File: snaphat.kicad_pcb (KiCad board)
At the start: 2 copper layers, 100 x 99.4 mm, 115 parts, among them J1 Conn_01x08_S8B-PH-K-S(LF)(SN), J10 P70-6000045R, J11 P70-6000045R, J12 P70-6000045R, J2 Conn_02x20_2214SM-40G-75-PCR, J3 Conn_01x02_B2B-PH-K-S(LF)(SN), J4 USB_C_USB4930-00-A, J5 Conn_01x03_MC34747, J6 Conn_01x04_SFV4R-3STBE1HLF/C, J7 Conn_01x04_SFV4R-3STBE1HLF/C, J8 P70-6000045R, J9 P70-6000045R, Q1 Q_BC817-25, Q2 Q_FDC6561AN, SW1 SW_B3FS-1050, SW2 SW_B3FS-1050, SW3 SW_B3FS-1050, SW4 SW_B3FS-1050, SW5 SW_B3FS-1050, SW6 SW_B3FS-1050, SW7 SW_B3FS-1050, SW8 SW_B3F-3150, SW9 1825232-1, U1 INA219BIDR, U2 MIC2250-1YD5-TR, U3 MCP73871T-2CCI/ML, U5 AP9101CAK6-ABTRG1, U6 LIS2DW12TR

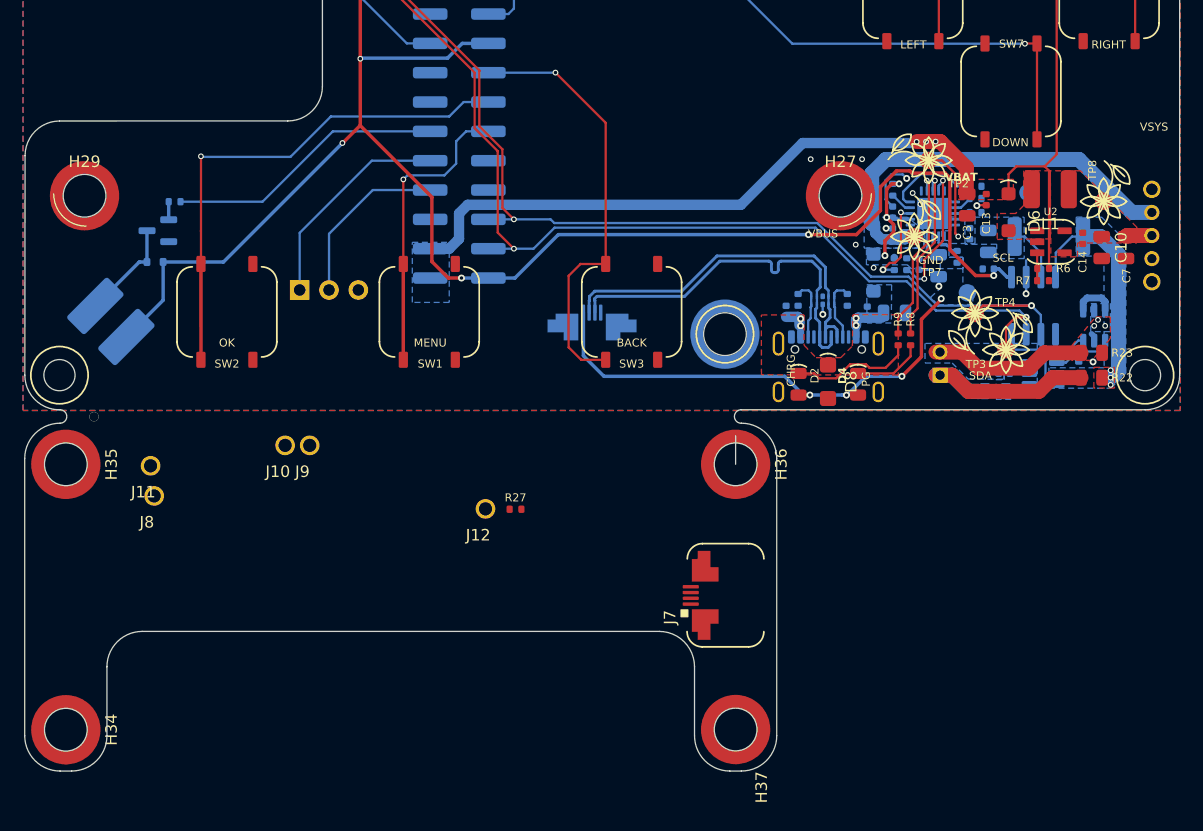
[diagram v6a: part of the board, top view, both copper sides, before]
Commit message: Route USB hat
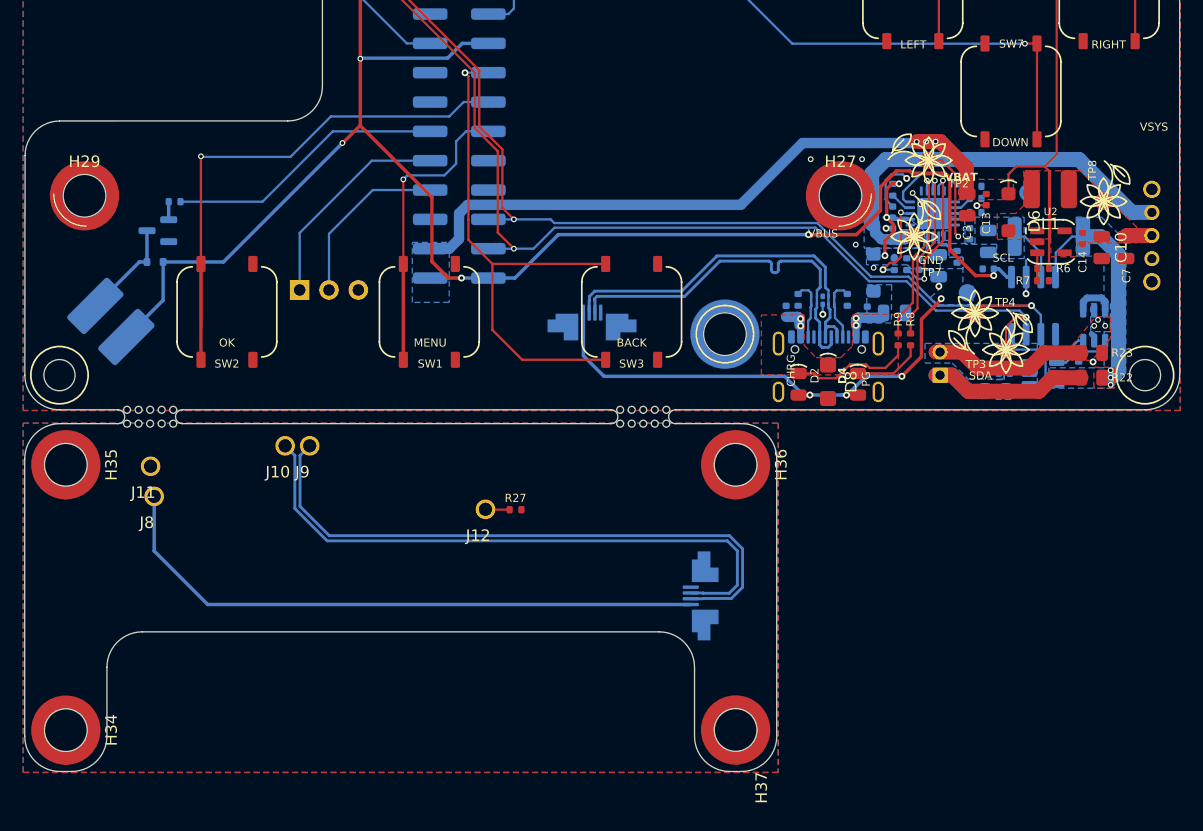
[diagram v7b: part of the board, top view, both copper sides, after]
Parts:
- added REF**: MouseBites_1.2mm, library:MouseBites_1.2mm, F.Cu at (199.6, 129.1)
- added REF**: MouseBites_1.2mm, library:MouseBites_1.2mm, F.Cu at (154.7, 129.7)
- J7: moved to B.Cu
- turned J7 to -90 degrees
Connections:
- J7 pad 1: /VBUS_EXT -> /GND_EXT
- J7 pad 2: /USBC_EXT_DATA_N -> /USBC_EXT_DATA_P
- J7 pad 3: /USBC_EXT_DATA_P -> /USBC_EXT_DATA_N
- J7 pad 4: /GND_EXT -> /VBUS_EXT
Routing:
- net /USBC_EXT_DATA_N: track 0.00 -> 53.7 mm
- net /VBUS_EXT: track 0.00 -> 53.1 mm
- net /USBC_EXT_DATA_P: track 0.00 -> 52.9 mm
- net /GND_EXT: track 0.00 -> 52.6 mm
- net /BTN_B: track 37.7 -> 46.0 mm
- net /OTG_EXT: track 0.00 -> 2.10 mm
- net (no net): vias 1 -> 0
- added copper zone on B.Cu, net /GND_EXT
- added copper zone on F.Cu, net /GND_EXT
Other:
- outline, holes or cut-outs redrawn

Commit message: Layout nits
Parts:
- added TP15: TestPoint, library:TestPoint_Pad_D1.5mm, B.Cu at (153.7, 138.9)
- added TP16: TestPoint, library:TestPoint_Pad_D1.5mm, B.Cu at (157.9, 140.6)
- added TP17: TestPoint, library:TestPoint_Pad_D1.5mm, B.Cu at (189.7, 137.1)
- TP2: moved to B.Cu
- moved TP11 20.2 mm to (213.6, 112.9), turned to 0 degrees
- moved TP2 10.5 mm to (235.1, 109.4)
- moved REF** 2.28 mm to (197.4, 129.7)
- moved TP6 1.12 mm to (228.7, 119.4), turned to 180 degrees
- moved TP4 0.30 mm to (228.9, 119.9)
- moved J1 0.08 mm to (170.0, 62.6)
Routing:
- net +3.3V: track 180.7 -> 185.9 mm
- net /I2C_SCL: track 107.4 -> 110.7 mm
- net /OTG_EXT: track 2.10 -> 5.29 mm
- net VBAT: track 13.5 -> 11.4 mm, vias 1 -> 0
- net /I2C_SDA: track 100.9 -> 102.7 mm
- net /BTN_A: track 49.9 -> 48.1 mm
- net +5V: track 119.7 -> 121.4 mm
- net /RPI_UART_TX: track 15.2 -> 16.1 mm
- net /USBC_EXT_DATA_P: track 52.9 -> 53.6 mm
- net /RPI_UART_RX: track 18.8 -> 19.4 mm
- net /BTN_MENU: track 31.3 -> 31.8 mm
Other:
- outline, holes or cut-outs redrawn
